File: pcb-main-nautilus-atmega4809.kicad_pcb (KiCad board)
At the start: 4 copper layers, 68.6 x 53.3 mm, 91 parts, among them J1 694106301002, J2 105017-0001, J3 FTSH-105-01-L-DV-007-K, J4 75844-101-06LF, J5 66951-006LF, J6 66951-010LF, J7 66951-008LF, J8 66951-008LF, Q1 BSS138PW, Q2 BSS138PW, Q3 BSS138PW, SW1 PTS645SH43SMTR92 LFS, U1 NCP1117-5.0_TO252, U2 AP2112K-3.3, U3 ATSAMD11D14A-SS, U4 ATmega4809-A

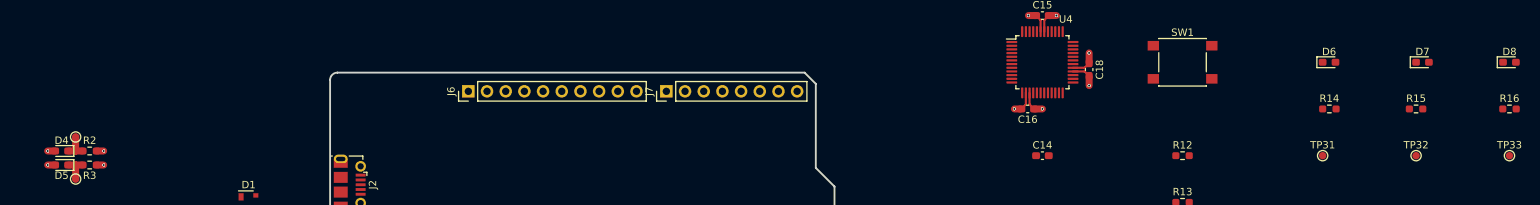
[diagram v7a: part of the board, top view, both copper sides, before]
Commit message: Arrange TX/RX indicators
Supports #4.
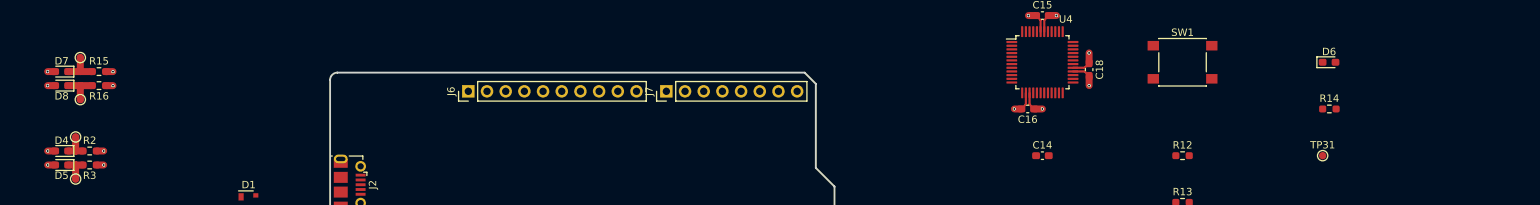
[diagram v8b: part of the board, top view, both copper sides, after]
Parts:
- moved D8 196.9 mm to (63.5, 98.4), turned to 180 degrees
- moved TP33 194.5 mm to (66.0, 100.3)
- moved R16 191.8 mm to (68.6, 98.4)
- moved D7 185.0 mm to (63.5, 96.5), turned to 180 degrees
- moved TP32 182.1 mm to (66.0, 94.6)
- moved R15 179.1 mm to (68.6, 96.5)
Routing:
- net Net-(D8-Pad1): track 0.00 -> 5.20 mm
- net Net-(D7-Pad1): track 0.00 -> 5.20 mm
- net /5V: track 16.8 -> 18.9 mm, vias 8 -> 10
- net /MCU/TX: track 1.96 -> 2.95 mm, vias 0 -> 1
- net /MCU/RX: track 1.96 -> 2.95 mm, vias 0 -> 1
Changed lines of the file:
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@@
   )
   (footprint "Resistor_SMD:R_0603_1608Metric_Pad0.98x0.95mm_HandSolder" (layer "F.Cu")
-    (at 260.35 101.6)
+    (at 68.58 98.425)
     (descr "Resistor SMD 0603 (1608 Metric), square (rectangular) end terminal, IPC_7351 nominal with elongated pad for handsoldering. (Body size source: IPC-SM-782 page 72, https://www.pcb-3d.com/wordpress/wp-content/uploads/ipc-sm-782a_amendment_1_and_2.pdf), generated with kicad-footprint-generator")
     (tags "resistor handsolder")
@@
     (property "Sheetname" "MCU")
     (attr smd)
-    (fp_text reference "R16" (at 0 -1.43) (layer "F.SilkS")
+    (fp_text reference "R16" (at 0 1.43) (layer "F.SilkS")
       (effects (font (size 1 1) (thickness 0.15)))
     )
@@
   )
   (footprint "LED_SMD:LED_0603_1608Metric_Pad1.05x0.95mm_HandSolder" (layer "F.Cu")
-    (at 248.525 95.25)
+    (at 63.5 96.52 180)
     (descr "LED SMD 0603 (1608 Metric), square (rectangular) end terminal, IPC_7351 nominal, (Body size source: http://www.tortai-tech.com/upload/download/2011102023233369053.pdf), generated with kicad-footprint-generator")
     (tags "LED handsolder")
@@
     (property "Sheetname" "MCU")
     (attr smd)
-    (fp_text reference "D7" (at 0 -1.43) (layer "F.SilkS")
+    (fp_text reference "D7" (at 0 1.43) (layer "F.SilkS")
       (effects (font (size 1 1) (thickness 0.15)))
     )
@@
     (fp_line (start 0.8 0.4) (end 0.8 -0.4) (layer "F.Fab") (width 0.1))
     (fp_line (start -0.8 0.4) (end 0.8 0.4) (layer "F.Fab") (width 0.1))
-    (pad "1" smd roundrect (at -0.875 0) (size 1.05 0.95) (layers "F.Cu" "F.Paste" "F.Mask") (roundrect_rratio 0.25)
+    (pad "1" smd roundrect (at -0.875 0 180) (size 1.05 0.95) (layers "F.Cu" "F.Paste" "F.Mask") (roundrect_rratio 0.25)
       (net 17 "Net-(D7-Pad1)") (pinfunction "K") (pintype "passive"))
-    (pad "2" smd roundrect (at 0.875 0) (size 1.05 0.95) (layers "F.Cu" "F.Paste" "F.Mask") (roundrect_rratio 0.25)
+    (pad "2" smd roundrect (at 0.875 0 180) (size 1.05 0.95) (layers "F.Cu" "F.Paste" "F.Mask") (roundrect_rratio 0.25)
       (net 4 "/5V") (pinfunction "A") (pintype "passive"))
     (model "${KICAD6_3DMODEL_DIR}/LED_SMD.3dshapes/LED_0603_1608Metric.wrl"
@@
   )
   (footprint "TestPoint:TestPoint_Pad_D1.0mm" (layer "F.Cu")
-    (at 260.35 107.95)
+    (at 66.04 100.33)
     (descr "SMD pad as test Point, diameter 1.0mm")
     (tags "test point SMD pad")
@@
     (property "Sheetname" "MCU")
     (attr exclude_from_pos_files)
-    (fp_text reference "TP33" (at 0 -1.448) (layer "F.SilkS")
+    (fp_text reference "TP33" (at 0 -1.448) (layer "F.SilkS") hide
       (effects (font (size 1 1) (thickness 0.15)))
     )
@@
   )
   (footprint "TestPoint:TestPoint_Pad_D1.0mm" (layer "F.Cu")
-    (at 247.65 107.95)
+    (at 66.04 94.615)
     (descr "SMD pad as test Point, diameter 1.0mm")
     (tags "test point SMD pad")
@@
     (property "Sheetname" "MCU")
     (attr exclude_from_pos_files)
-    (fp_text reference "TP32" (at 0 -1.448) (layer "F.SilkS")
+    (fp_text reference "TP32" (at 0 -1.448) (layer "F.SilkS") hide
       (effects (font (size 1 1) (thickness 0.15)))
     )
@@
   )
   (footprint "LED_SMD:LED_0603_1608Metric_Pad1.05x0.95mm_HandSolder" (layer "F.Cu")
-    (at 260.35 95.25)
+    (at 63.5 98.425 180)
     (descr "LED SMD 0603 (1608 Metric), square (rectangular) end terminal, IPC_7351 nominal, (Body size source: http://www.tortai-tech.com/upload/download/2011102023233369053.pdf), generated with kicad-footprint-generator")
     (tags "LED handsolder")
@@
     (fp_line (start 0.8 0.4) (end 0.8 -0.4) (layer "F.Fab") (width 0.1))
     (fp_line (start -0.8 0.4) (end 0.8 0.4) (layer "F.Fab") (width 0.1))
-    (pad "1" smd roundrect (at -0.875 0) (size 1.05 0.95) (layers "F.Cu" "F.Paste" "F.Mask") (roundrect_rratio 0.25)
+    (pad "1" smd roundrect (at -0.875 0 180) (size 1.05 0.95) (layers "F.Cu" "F.Paste" "F.Mask") (roundrect_rratio 0.25)
       (net 18 "Net-(D8-Pad1)") (pinfunction "K") (pintype "passive"))
-    (pad "2" smd roundrect (at 0.875 0) (size 1.05 0.95) (layers "F.Cu" "F.Paste" "F.Mask") (roundrect_rratio 0.25)
+    (pad "2" smd roundrect (at 0.875 0 180) (size 1.05 0.95) (layers "F.Cu" "F.Paste" "F.Mask") (roundrect_rratio 0.25)
       (net 4 "/5V") (pinfunction "A") (pintype "passive"))
     (model "${KICAD6_3DMODEL_DIR}/LED_SMD.3dshapes/LED_0603_1608Metric.wrl"
@@
   )
   (footprint "Resistor_SMD:R_0603_1608Metric_Pad0.98x0.95mm_HandSolder" (layer "F.Cu")
-    (at 247.65 101.6)
+    (at 68.58 96.52)
     (descr "Resistor SMD 0603 (1608 Metric), square (rectangular) end terminal, IPC_7351 nominal with elongated pad for handsoldering. (Body size source: IPC-SM-782 page 72, https://www.pcb-3d.com/wordpress/wp-content/uploads/ipc-sm-782a_amendment_1_and_2.pdf), generated with kicad-footprint-generator")
     (tags "resistor handsolder")
@@
   (segment (start 197.7125 88.9) (end 198.755 88.9) (width 0.95) (layer "F.Cu") (net 4))
   (segment (start 193.9875 101.6) (end 193.04 101.6) (width 0.95) (layer "F.Cu") (net 4))
+  (segment (start 62.625 98.425) (end 61.595 98.425) (width 0.95) (layer "F.Cu") (net 4))
   (segment (start 202.5875 96.5) (end 203.2 97.1125) (width 0.3) (layer "F.Cu") (net 4))
   (segment (start 203.2 97.1125) (end 203.2 98.425) (width 0.95) (layer "F.Cu") (net 4))
@@
   (segment (start 197.1 91.0875) (end 197.1 89.5125) (width 0.3) (layer "F.Cu") (net 4))
   (segment (start 115.6825 64.215) (end 114.38 64.215) (width 0.95) (layer "F.Cu") (net 4))
+  (segment (start 62.625 96.52) (end 61.595 96.52) (width 0.95) (layer "F.Cu") (net 4))
   (via (at 198.755 88.9) (size 0.4572) (drill 0.254) (layers "F.Cu" "B.Cu") (net 4))
   (via (at 114.38 64.215) (size 0.4572) (drill 0.254) (layers "F.Cu" "B.Cu") (net 4))
   (via (at 193.04 101.6) (size 0.4572) (drill 0.254) (layers "F.Cu" "B.Cu") (net 4))
+  (via (at 61.595 96.52) (size 0.4572) (drill 0.254) (layers "F.Cu" "B.Cu") (net 4))
   (via (at 203.2 98.425) (size 0.4572) (drill 0.254) (layers "F.Cu" "B.Cu") (net 4))
   (via (at 110.49 78.74) (size 0.4572) (drill 0.254) (layers "F.Cu" "B.Cu") (net 4))
   (via (at 114.38 55.325) (size 0.4572) (drill 0.254) (layers "F.Cu" "B.Cu") (net 4))
   (via (at 61.595 107.315) (size 0.4572) (drill 0.254) (layers "F.Cu" "B.Cu") (net 4))
+  (via (at 61.595 98.425) (size 0.4572) (drill 0.254) (layers "F.Cu" "B.Cu") (net 4))
   (via (at 114.38 59.77) (size 0.4572) (drill 0.254) (layers "F.Cu" "B.Cu") (net 4))
   (segment (start 62.625 109.22) (end 61.595 109.22) (width 0.95) (layer "F.Cu") (net 5))
@@
   (segment (start 64.375 109.22) (end 65.405 109.22) (width 0.95) (layer "F.Cu") (net 14))
   (segment (start 65.405 109.22) (end 65.405 111.125) (width 0.95) (layer "F.Cu") (net 14))
+  (segment (start 66.04 96.52) (end 67.6675 96.52) (width 0.95) (layer "F.Cu") (net 17))
+  (segment (start 64.375 96.52) (end 66.04 96.52) (width 0.95) (layer "F.Cu") (net 17))
+  (segment (start 66.04 96.52) (end 66.04 94.615) (width 0.95) (layer "F.Cu") (net 17))
+  (segment (start 66.04 98.425) (end 67.6675 98.425) (width 0.95) (layer "F.Cu") (net 18))
+  (segment (start 66.04 98.425) (end 66.04 100.33) (width 0.95) (layer "F.Cu") (net 18))
+  (segment (start 64.375 98.425) (end 66.04 98.425) (width 0.95) (layer "F.Cu") (net 18))
   (segment (start 137.795 73.025) (end 137.795 71.625) (width 0.6) (layer "F.Cu") (net 20))
   (segment (start 137.795 73.025) (end 140.44 73.025) (width 0.6) (layer "F.Cu") (net 20))
@@
   (segment (start 109.37 62.245) (end 109.1075 62.5075) (width 0.45) (layer "F.Cu") (net 51))
   (segment (start 111.065 62.245) (end 109.37 62.245) (width 0.45) (layer "F.Cu") (net 51))
+  (segment (start 69.4925 98.425) (end 70.485 98.425) (width 0.95) (layer "F.Cu") (net 52))
   (segment (start 113.725 61.595) (end 115.6825 61.595) (width 0.45) (layer "F.Cu") (net 52))
+  (via (at 70.485 98.425) (size 0.4572) (drill 0.254) (layers "F.Cu" "B.Cu") (net 52))
   (segment (start 109.37 57.8) (end 109.1075 58.0625) (width 0.45) (layer "F.Cu") (net 53))
   (segment (start 111.065 57.8) (end 109.37 57.8) (width 0.45) (layer "F.Cu") (net 53))
+  (segment (start 69.4925 96.52) (end 70.485 96.52) (width 0.95) (layer "F.Cu") (net 54))
   (segment (start 113.725 57.15) (end 115.6825 57.15) (width 0.45) (layer "F.Cu") (net 54))
+  (via (at 70.485 96.52) (size 0.4572) (drill 0.254) (layers "F.Cu" "B.Cu") (net 54))
 )
